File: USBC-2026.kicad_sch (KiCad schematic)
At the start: 0 parts

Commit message: Imported TPS25752A IC into KiCad
added IC symbol and footprint into kicad project
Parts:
- added IC1: TPS25752ASRSMR, QFN40P400X400X100-33N-D, symbol TPS25752ASRSMR:TPS25752ASRSMR
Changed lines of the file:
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@@
 	(generator_version "10.0")
 	(paper "A4")
+	(symbol
+		(lib_id "TPS25752ASRSMR:TPS25752ASRSMR")
+		(at 77.47 73.66 0)
+		(unit 1)
+		(body_style 1)
+		(exclude_from_sim no)
+		(in_bom yes)
+		(on_board yes)
+		(in_pos_files yes)
+		(dnp no)
+		(fields_autoplaced yes)
+		(property "Reference" "IC1"
+			(at 128.27 67.2398 0)
+			(show_name no)
+			(do_not_autoplace no)
+			(effects
+				(font
+					(size 1.27 1.27)
+				)
+			)
+		)
+		(property "Value" "TPS25752ASRSMR"
+			(at 128.27 69.7798 0)
+			(show_name no)
+			(do_not_autoplace no)
+			(effects
+				(font
+					(size 1.27 1.27)
+				)
+			)
+		)
+		(property "Footprint" "QFN40P400X400X100-33N-D"
+			(at 119.38 155.88 0)
+			(hide yes)
+			(show_name no)
+			(do_not_autoplace no)
+			(effects
+				(font
+					(size 1.27 1.27)
+				)
+				(justify left top)
+			)
+		)
+		(property "Datasheet" "https://www.ti.com/lit/ds/symlink/tps25752a.pdf?ts=1785223982749&ref_url=https%253A%252F%252Fwww.ti.com%252Fproduct%252FTPS25752A"
+			(at 119.38 255.88 0)
+			(hide yes)
+			(show_name no)
+			(do_not_autoplace no)
+			(effects
+				(font
+					(size 1.27 1.27)
+				)
+				(justify left top)
+			)
+		)
+		(property "Description" "USB Interface IC TPS25752A Source-only USB-C Power Delivery 3.2 controller"
+			(at 77.47 73.66 0)
+			(hide yes)
+			(show_name no)
+			(do_not_autoplace no)
+			(effects
+				(font
+					(size 1.27 1.27)
+				)
+			)
+		)
+		(property "Height" "1"
+			(at 119.38 455.88 0)
+			(hide yes)
+			(show_name no)
+			(do_not_autoplace no)
+			(effects
+				(font
+					(size 1.27 1.27)
+				)
+				(justify left top)
+			)
+		)
+		(property "Mouser Part Number" ""
+			(at 119.38 555.88 0)
+			(hide yes)
+			(show_name no)
+			(do_not_autoplace no)
+			(effects
+				(font
+					(size 1.27 1.27)
+				)
+				(justify left top)
+			)
+		)
+		(property "Mouser Price/Stock" ""
+			(at 119.38 655.88 0)
+			(hide yes)
+			(show_name no)
+			(do_not_autoplace no)
+			(effects
+				(font
+					(size 1.27 1.27)
+				)
+				(justify left top)
+			)
+		)
+		(property "Manufacturer_Name" "Texas Instruments"
+			(at 119.38 755.88 0)
+			(hide yes)
+			(show_name no)
+			(do_not_autoplace no)
+			(effects
+				(font
+					(size 1.27 1.27)
+				)
+				(justify left top)
+			)
+		)
+		(property "Manufacturer_Part_Number" "TPS25752ASRSMR"
+			(at 119.38 855.88 0)
+			(hide yes)
+			(show_name no)
+			(do_not_autoplace no)
+			(effects
+				(font
+					(size 1.27 1.27)
+				)
+				(justify left top)
+			)
+		)
+		(pin "8"
+		)
+		(pin "24"
+		)
+		(pin "12"
+		)
+		(pin "2"
+		)
+		(pin "4"
+		)
+		(pin "6"
+		)
+		(pin "1"
+		)
+		(pin "7"
+		)
+		(pin "9"
+		)
+		(pin "5"
+		)
+		(pin "26"
+		)
+		(pin "25"
+		)
+		(pin "11"
+		)
+		(pin "3"
+		)
+		(pin "10"
+		)
+		(pin "14"
+		)
+		(pin "21"
+		)
+		(pin "22"
+		)
+		(pin "17"
+		)
+		(pin "20"
+		)
+		(pin "23"
+		)
+		(pin "16"
+		)
+		(pin "19"
+		)
+		(pin "18"
+		)
+		(pin "15"
+		)
+		(pin "13"
+		)
+		(pin "29"
+		)
+		(pin "32"
+		)
+		(pin "27"
+		)
+		(pin "31"
+		)
+		(pin "30"
+		)
+		(pin "33"
+		)
+		(pin "28"
+		)
+		(instances
+			(project "USBC-2026"
+				(path "/0c056c42-d02c-4bee-adc4-fcbb18375f33"
+					(reference "IC1")
+					(unit 1)
+				)
+			)
+		)
+	)
 	(sheet_instances
 		(path "/"

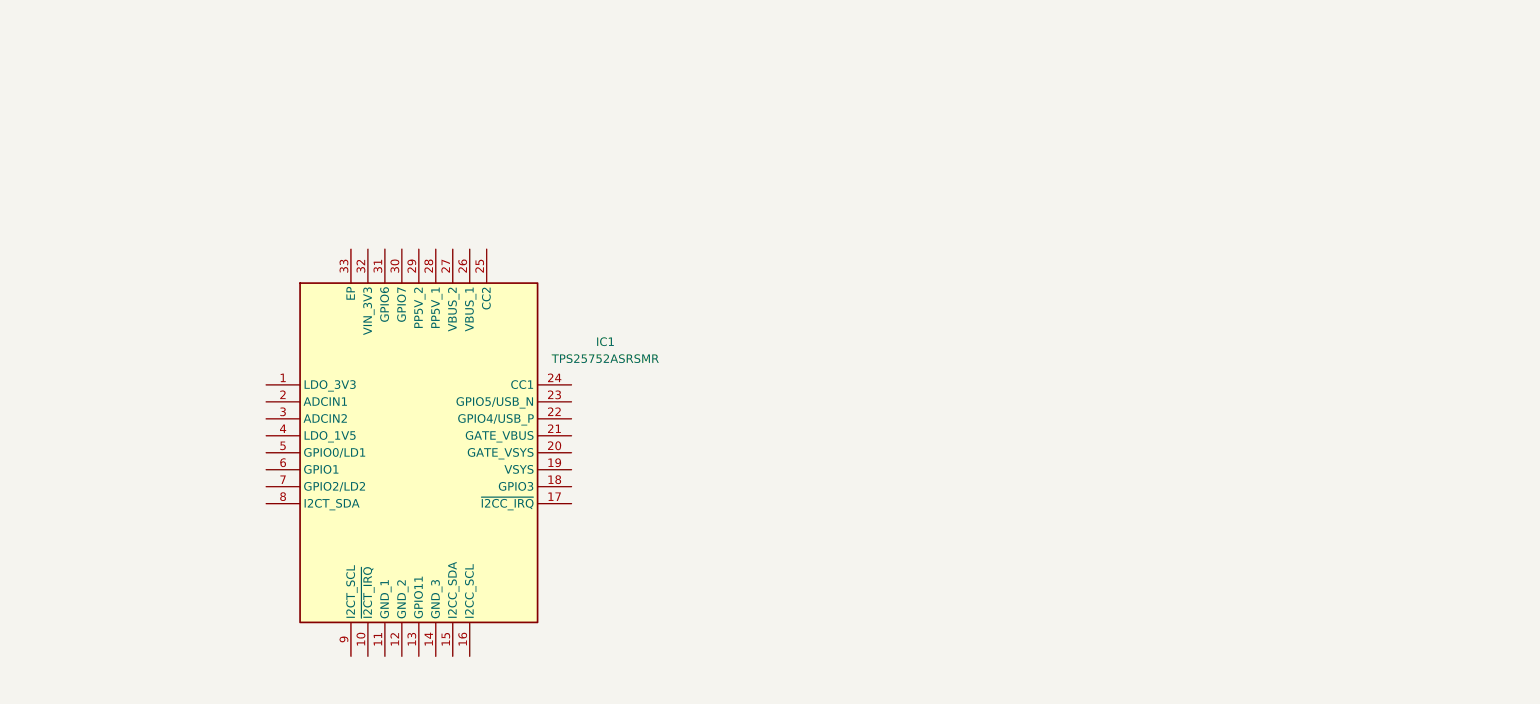
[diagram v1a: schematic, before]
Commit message: Added IC Connections + USBC 3.2 Port
connected up USBC controller IC according to datasheet's example schematic
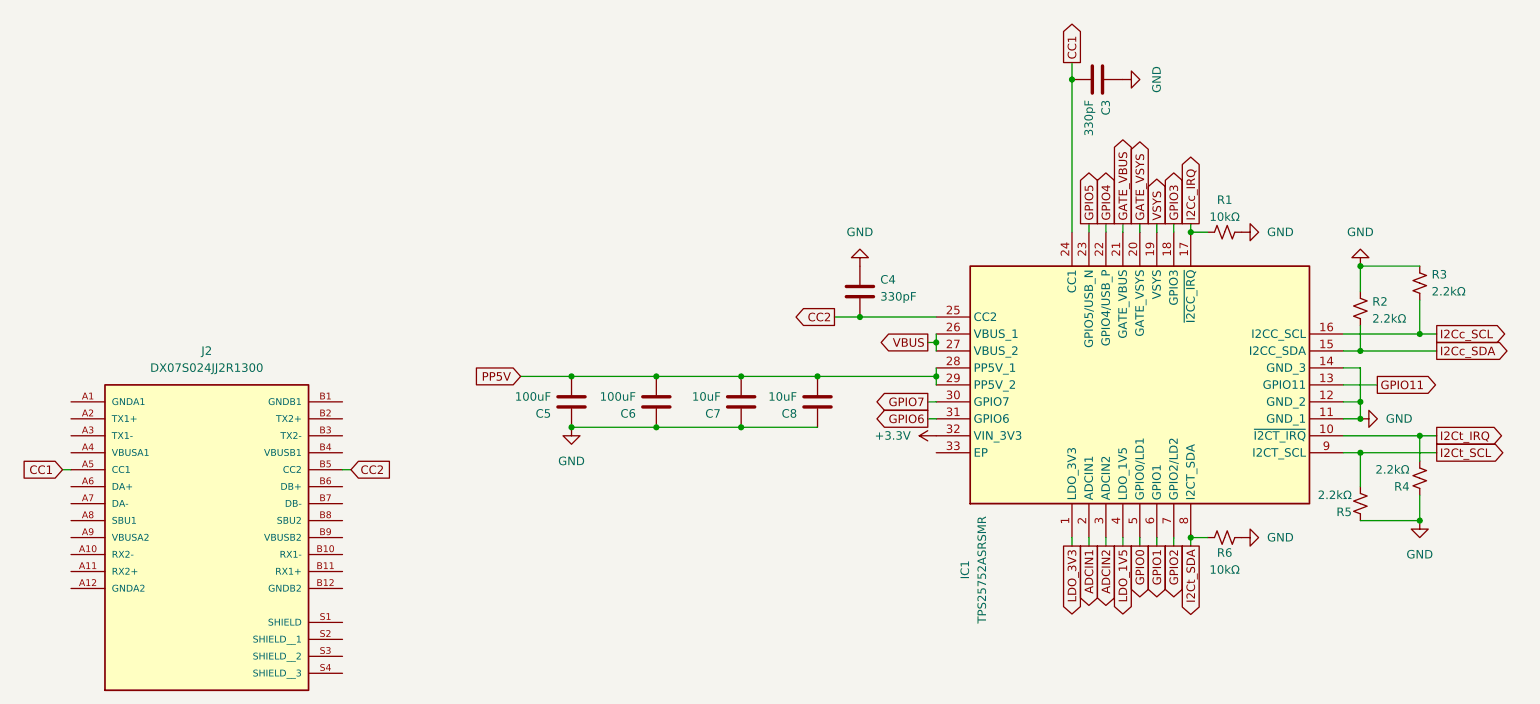
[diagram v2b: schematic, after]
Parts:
- added C3, C4: 330pF, Package_TO_SOT_SMD:SOT-23-5, symbol Device:C
- added C5, C6: 100uF, Package_TO_SOT_SMD:SOT-23-5, symbol Device:C
- added C7, C8: 10uF, Package_TO_SOT_SMD:SOT-23-5, symbol Device:C
- added J2: DX07S024JJ2R1300, DX07S024JJ2R1300:JAE_DX07S024JJ2R1300, symbol DX07S024JJ2R1300:DX07S024JJ2R1300
- added R1, R6: 10kΩ, Package_DIP:DIP-8_W7.62mm, symbol Device:R_Small_US
- added R2, R3, R4, R5: 2.2kΩ, Package_DIP:DIP-8_W7.62mm, symbol Device:R_Small_US
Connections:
- net LDO_3V3: now reaches IC1.1 (LDO_3V3)
- net I2Ct_IRQ: now reaches IC1.10 (~{I2CT_IRQ})
- net I2Ct_IRQ: now also R4.1
- net GND: now reaches IC1.11 (GND_1)
- net GND: now also IC1.12 (GND_2), IC1.14 (GND_3), C3.2, C4.2, C5.2, C6.2, C7.2, C8.2, R1.2, R2.2, R3.2, R4.2, R5.2, R6.2
- net GPIO11: now reaches IC1.13 (GPIO11)
- net I2Cc_SDA: now reaches IC1.15 (I2CC_SDA)
- net I2Cc_SDA: now also R2.1
- net I2Cc_SCL: now reaches IC1.16 (I2CC_SCL)
- net I2Cc_SCL: now also R3.1
- net I2Cc_IRQ: now reaches IC1.17 (~{I2CC_IRQ})
- net I2Cc_IRQ: now also R1.1
- net GPIO3: now reaches IC1.18 (GPIO3)
- net VSYS: now reaches IC1.19 (VSYS)
- net ADCIN1: now reaches IC1.2 (ADCIN1)
- net GATE_VSYS: now reaches IC1.20 (GATE_VSYS)
- net GATE_VBUS: now reaches IC1.21 (GATE_VBUS)
- net GPIO4: now reaches IC1.22 (GPIO4/USB_P)
- net GPIO5: now reaches IC1.23 (GPIO5/USB_N)
- net CC1: now reaches IC1.24 (CC1)
- net CC1: now also C3.1, J2.A5 (CC1)
- net CC2: now reaches IC1.25 (CC2)
- net CC2: now also C4.1, J2.B5 (CC2)
- net VBUS: now reaches IC1.26 (VBUS_1)
- net VBUS: now also IC1.27 (VBUS_2)
- net PP5V: now reaches IC1.28 (PP5V_1)
- net PP5V: now also IC1.29 (PP5V_2), C5.1, C6.1, C7.1, C8.1
- net ADCIN2: now reaches IC1.3 (ADCIN2)
- net GPIO7: now reaches IC1.30 (GPIO7)
- net GPIO6: now reaches IC1.31 (GPIO6)
- net +3.3V: now reaches IC1.32 (VIN_3V3)
- net LDO_1V5: now reaches IC1.4 (LDO_1V5)
- net GPIO0: now reaches IC1.5 (GPIO0/LD1)
- net GPIO1: now reaches IC1.6 (GPIO1)
- net GPIO2: now reaches IC1.7 (GPIO2/LD2)
- net I2Ct_SDA: now reaches IC1.8 (I2CT_SDA)
- net I2Ct_SDA: now also R6.1
- net I2Ct_SCL: now reaches IC1.9 (I2CT_SCL)
- net I2Ct_SCL: now also R5.1
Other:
- moved on the sheet: IC1
